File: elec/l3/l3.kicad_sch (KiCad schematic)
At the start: 2 parts

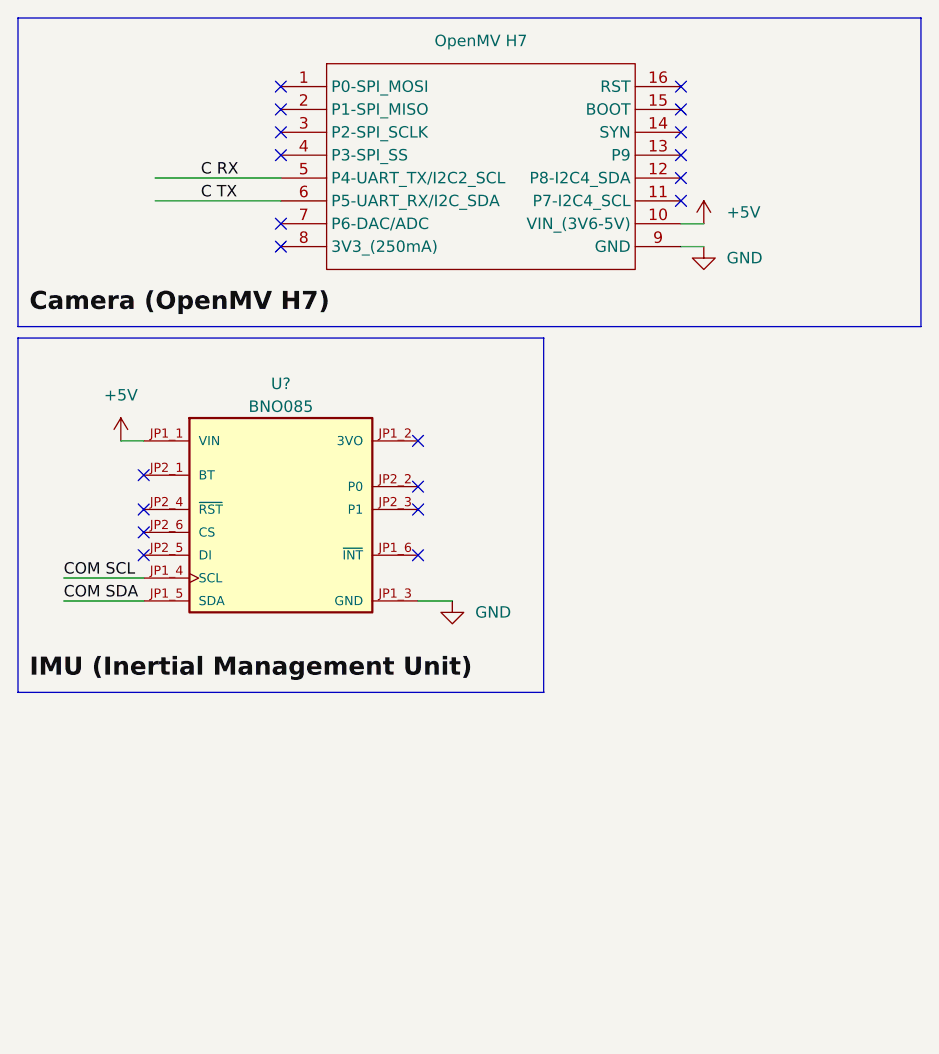
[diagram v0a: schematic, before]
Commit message: producion l1, fucked l2 need to redo, todo: l2,l3
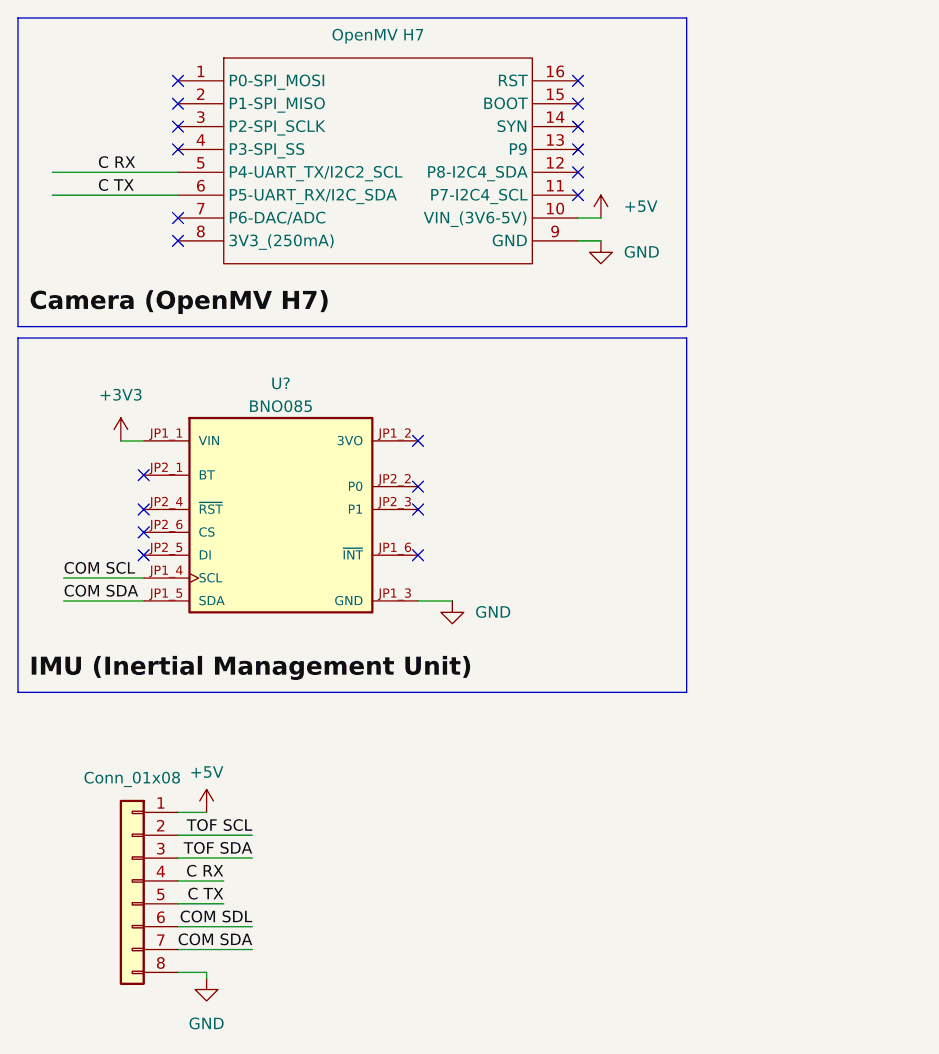
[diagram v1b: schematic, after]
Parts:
- added J1: Conn_01x08, Connector_PinSocket_2.54mm:PinSocket_1x08_P2.54mm_Vertical, symbol Connector_Generic:Conn_01x08
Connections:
- net +5V: now also J1.1 (Pin_1); no longer U?.JP1_1 (VIN)
- net C RX: now also J1.4 (Pin_4)
- net C TX: now also J1.5 (Pin_5)
- net COM SDA: now also J1.7 (Pin_7)
- net GND: now also J1.8 (Pin_8)
- new net +3V3: U?.JP1_1 (VIN)
- new net COM SDL: J1.6 (Pin_6)
- new net TOF SCL: J1.2 (Pin_2)
- new net TOF SDA: J1.3 (Pin_3)

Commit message: 2024-02-28 production
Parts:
- removed U?: OpenMV H7, footprints:openmv, symbol OpenMV:OpenMV_H7
- added D1: D_Schottky, Diode_SMD:D_0603_1608Metric_Pad1.05x0.95mm_HandSolder, symbol Device:D_Schottky
- added H1, H10, H11, H12, H2, H3, H4, H5, H6, H7, H8, H9: MountingHole_Pad, MountingHole:MountingHole_3mm_Pad_Via, symbol Mechanical:MountingHole_Pad
- added J2, J3, J4, J6: Conn_01x06, Connector_PinSocket_2.54mm:PinSocket_1x06_P2.54mm_Vertical, symbol Connector_Generic:Conn_01x06
- added J5: Conn_01x32, l3:OpenMV_RT, symbol Connector_Generic:Conn_01x32
- added R1, R2, R3, R4: 3K3, l2:res0603, symbol Device:R
- added U3: MOUDLE-SEEEDUINO-XIAO-ESP32C3, l2:Seeeduino XIAO SAMD 21 TFT, symbol MOUDLE-SEEEDUINO-XIAO-ESP32C3:MOUDLE-SEEEDUINO-XIAO-ESP32C3
- U?: footprint footprints:bno085 -> l3:bno085
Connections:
- net +3V3 is gone; now on net +5V: U?.JP1_1 (VIN)
- net COM SDL is gone; now on net COM SCL: J1.6 (Pin_6)
- net +5V: now also D1.2 (A), J2.1 (Pin_1), J3.1 (Pin_1), J4.1 (Pin_1), J5.30 (Pin_30), J6.1 (Pin_1), R1.1, R2.1, R3.1, R4.1
- net C RX: now also J5.4 (Pin_4)
- net C TX: now also J5.6 (Pin_6)
- net COM SCL: now also R3.2
- net COM SDA: now also R4.2
- net GND: now also J2.2 (Pin_2), J3.2 (Pin_2), J4.2 (Pin_2), J5.31 (Pin_31), J6.2 (Pin_2), U3.13 (GND)
- net TOF SCL: now also J2.3 (Pin_3), J3.3 (Pin_3), J4.3 (Pin_3), J6.3 (Pin_3), R1.2
- net TOF SDA: now also J2.4 (Pin_4), J3.4 (Pin_4), J4.4 (Pin_4), J6.4 (Pin_4), R2.2
- new net: D1.1 (K), U3.14 (5V)
- new net XSHUT f: J3.6 (Pin_6), U3.4 (PA11_A3_D3)
- new net XSHUT n: J2.6 (Pin_6), U3.1 (PA02_A0_D0)
- new net XSHUT s: J4.6 (Pin_6), U3.3 (PA10_A2_D2)
- new net XSHUT w: J6.6 (Pin_6), U3.2 (PA4_A1_D1)
- no-connect marks 20 -> 59
